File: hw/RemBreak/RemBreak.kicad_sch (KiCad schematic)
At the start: 7 parts, among them IC1 MAX17049G+T10, J1 Conn_01x03, J2 Conn_01x03, J6 Conn_01x02, SW1 SW_SPST, U1 SeeeduinoXIAO

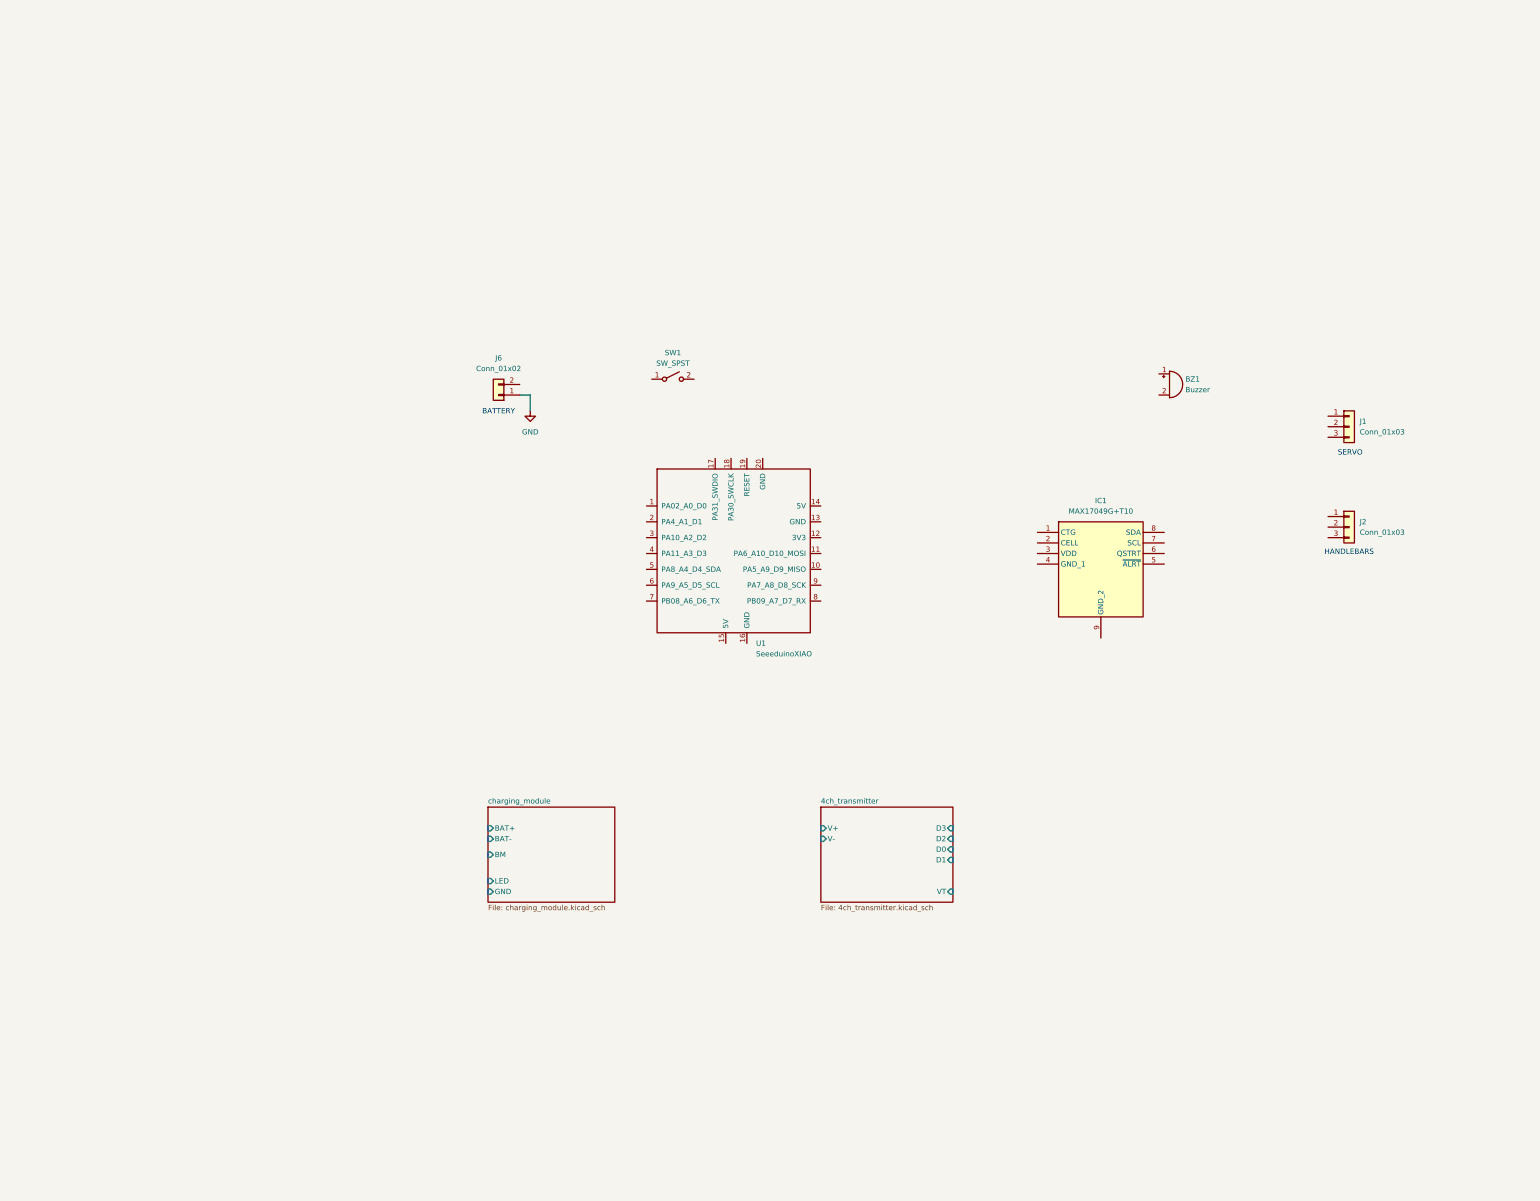
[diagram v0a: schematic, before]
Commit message: first version of the remote break main board
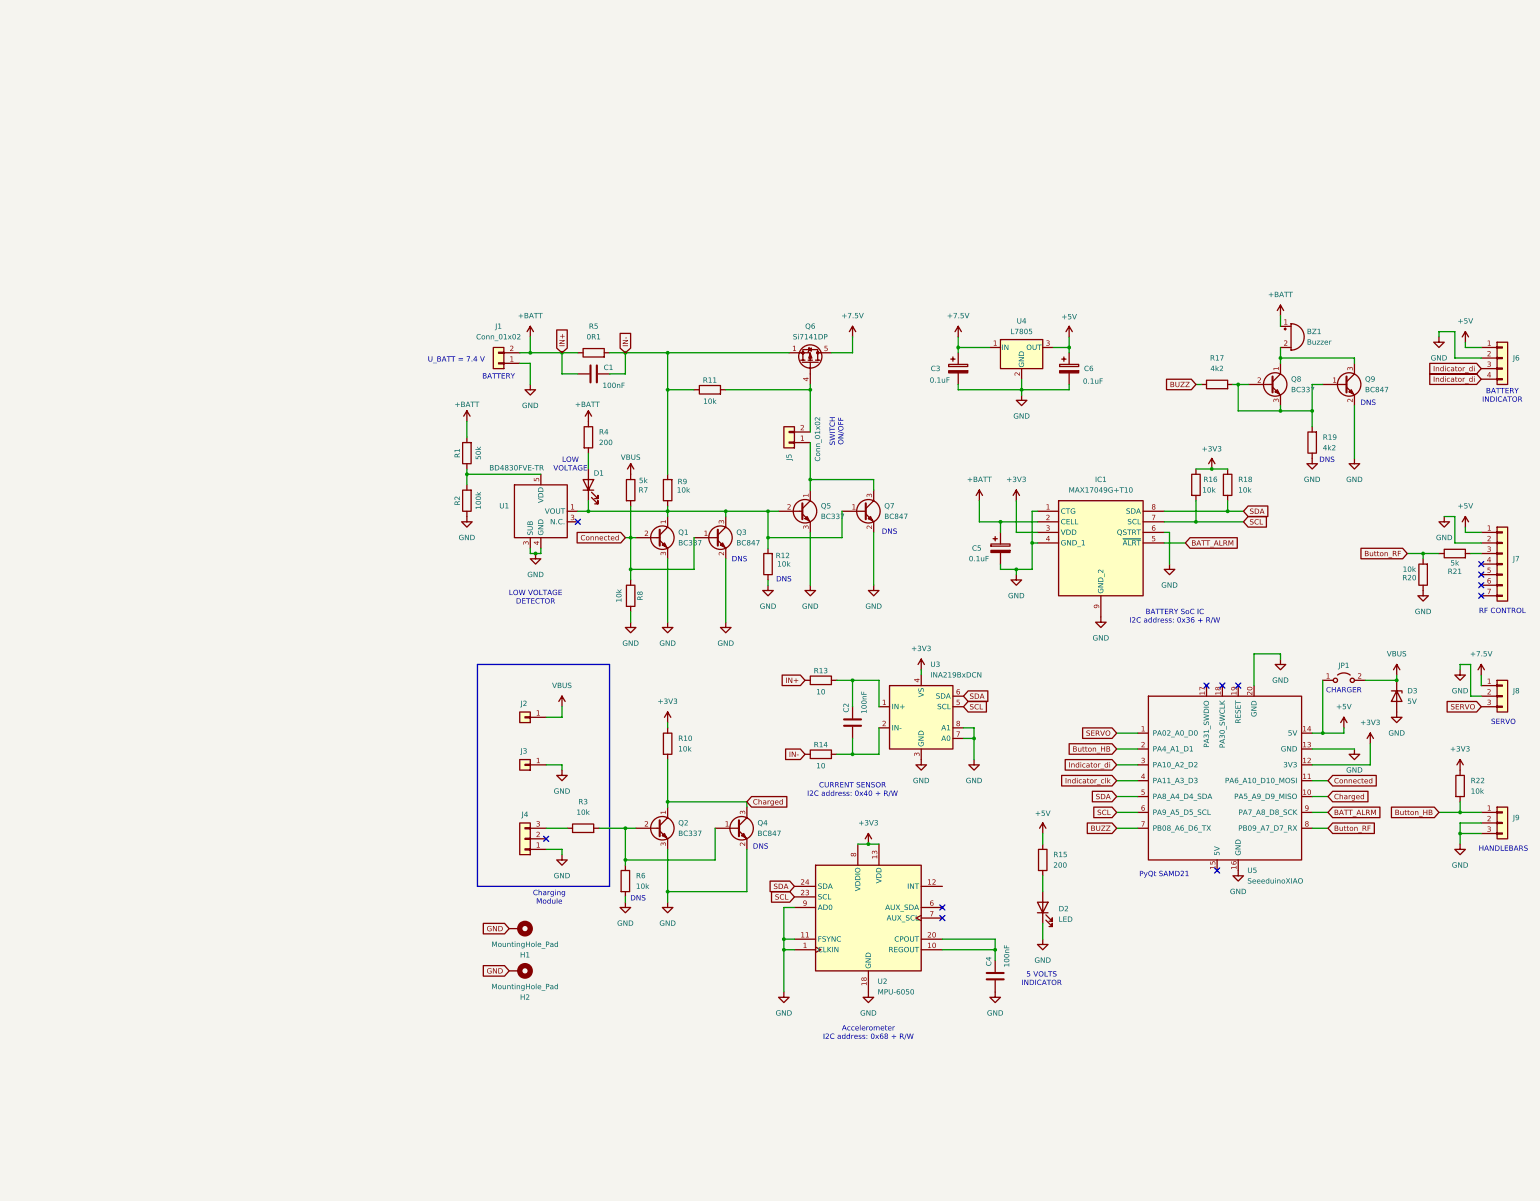
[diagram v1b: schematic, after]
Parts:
- removed SW1: SW_SPST, symbol Switch:SW_SPST
- added C1, C2, C4: 100nF, symbol Device:C
- added C3, C5, C6: 0.1uF, symbol Device:C_Polarized
- added D1, D2: LED, symbol Device:LED
- added D3: 5V, symbol Device:D_Zener
- added H1, H2: MountingHole_Pad, symbol Mechanical:MountingHole_Pad
- added J2, J3: Conn_01x01, symbol Connector_Generic:Conn_01x01
- added J4: Conn_01x03, symbol Connector_Generic:Conn_01x03
- added J5: Conn_01x02, symbol Connector_Generic:Conn_01x02
- added J6: Conn_01x04, symbol Connector_Generic:Conn_01x04
- added J7: Conn_01x07, symbol Connector_Generic:Conn_01x07
- added JP1: Jumper_2_Open, symbol Jumper:Jumper_2_Open
- added Q1, Q2, Q5, Q8: BC337, Package_TO_SOT_THT:TO-92_Inline, symbol Transistor_BJT:BC337
- added Q3, Q4, Q7, Q9: BC847, Package_TO_SOT_SMD:SOT-23, symbol Transistor_BJT:BC847
- added Q6: Si7141DP, Package_SO:PowerPAK_SO-8_Single, symbol Transistor_FET:Si7141DP
- added R1: 50k, symbol Device:R
- added R10, R11, R12, R16, R18, R20, R22, R3, R6, R8, R9: 10k, symbol Device:R
- added R13, R14: 10, symbol Device:R
- added R15, R4: 200, symbol Device:R
- added R17, R19: 4k2, symbol Device:R
- added R2: 100k, symbol Device:R
- added R21, R7: 5k, symbol Device:R
- added R5: 0R1, symbol Device:R
- added U1: BD4830FVE-TR, Package_TO_SOT_SMD:VSOF5, symbol dodo-power:BD4830FVE-TR
- added U2: MPU-6050, Sensor_Motion:InvenSense_QFN-24_4x4mm_P0.5mm, symbol Sensor_Motion:MPU-6050
- added U3: INA219BxDCN, Package_TO_SOT_SMD:SOT-23-8, symbol Analog_ADC:INA219BxDCN
- added U4: L7805, symbol Regulator_Linear:L7805
- renumbered J6 to J1, J1 to J8, J2 to J9, U1 to U5
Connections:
- net GND: now also IC1.1 (CTG), IC1.4 (GND_1), IC1.6 (QSTRT), IC1.9 (GND_2), J8.2 (Pin_2), J9.2 (Pin_2), J9.3 (Pin_3), U5.13 (GND), U5.16 (GND), U5.20 (GND), C3.2, C4.1, C5.2, C6.2, D2.1 (K), D3.2 (A), H1.1, H2.1, J3.1 (Pin_1), J4.1 (Pin_1), J6.2 (Pin_2), J7.2 (Pin_2), Q1.3 (E), Q2.3 (E), Q3.2 (E), Q4.2 (E), Q5.3 (E), Q7.2 (E), Q9.2 (E), R12.1, R19.1, R2.1, R20.1, R6.2, R8.2, U1.3 (SUB), U1.4 (GND), U2.1 (CLKIN), U2.11 (FSYNC), U2.18 (GND), U2.9 (AD0), U3.3 (GND), U3.7 (A0), U3.8 (A1), U4.2 (GND)
- net +BATT: now reaches BZ1.1 (-)
- net +BATT: now also IC1.2 (CELL), J1.2 (Pin_2), C1.1, C5.1, R1.2, R13.1, R4.1, R5.1
- net at BZ1.2 (+): now also Q8.1 (C), Q9.3 (C)
- net SERVO: now reaches U5.1 (PA02_A0_D0)
- net SERVO: now also J8.3 (Pin_3)
- net Charged: now reaches U5.10 (PA5_A9_D9_MISO)
- net Charged: now also Q2.1 (C), Q4.3 (C), R10.2
- net Connected: now reaches U5.11 (PA6_A10_D10_MOSI)
- net Connected: now also Q1.2 (B), Q3.1 (B), R7.2, R8.1
- net +3V3: now reaches U5.12 (3V3)
- net +3V3: now also IC1.3 (VDD), R10.1, R16.1, R18.1, R22.1, U2.13 (VDD), U2.8 (VDDIO), U3.4 (VS)
- net +5V: now reaches U5.14 (5V)
- net +5V: now also C6.1, J6.1 (Pin_1), J7.1 (Pin_1), JP1.1 (A), R15.1, U4.3 (OUT)
- net Button_HB: now reaches U5.2 (PA4_A1_D1)
- net Button_HB: now also J9.1 (Pin_1), R22.2
- net Indicator_di: now reaches U5.3 (PA10_A2_D2)
- net Indicator_di: now also J6.3 (Pin_3), J6.4 (Pin_4)
- net Indicator_clk: now reaches U5.4 (PA11_A3_D3)
- net SDA: now reaches U5.5 (PA8_A4_D4_SDA)
- net SDA: now also IC1.8 (SDA), R18.2, U2.24 (SDA), U3.6 (SDA)
- net SCL: now reaches U5.6 (PA9_A5_D5_SCL)
- net SCL: now also IC1.7 (SCL), R16.2, U2.23 (SCL), U3.5 (SCL)
- net BUZZ: now reaches U5.7 (PB08_A6_D6_TX)
- net BUZZ: now also R17.1
- net Button_RF: now reaches U5.8 (PB09_A7_D7_RX)
- net Button_RF: now also R20.2, R21.1
- net BATT_ALRM: now reaches U5.9 (PA7_A8_D8_SCK)
- net BATT_ALRM: now also IC1.5 (~{ALRT})
- net +7.5V: now reaches J8.1 (Pin_1)
- net +7.5V: now also C3.1, Q6.5 (D), U4.1 (IN)
- new net: J4.3 (Pin_3), R3.1
- new net: Q2.2 (B), Q4.1 (B), R3.2, R6.1
- new net: D1.1 (K), Q1.1 (C), Q3.3 (C), Q5.2 (B), Q7.1 (B), R12.2, R9.1, U1.1 (VOUT)
- new net: J5.2 (Pin_2), Q6.4 (G), R11.2
- new net: C2.1, R14.2, U3.2 (IN-)
- new net: C2.2, R13.2, U3.1 (IN+)
- new net: D1.2 (A), R4.2
- new net: R1.1, R2.2, U1.5 (VDD)
- new net: J5.1 (Pin_1), Q5.1 (C), Q7.3 (C)
- new net: D2.2 (A), R15.2
- new net: J7.3 (Pin_3), R21.2
- new net: C4.2, U2.10 (REGOUT), U2.20 (CPOUT)
- new net: Q8.2 (B), Q8.3 (E), Q9.1 (B), R17.2, R19.2
- new net IN-: C1.2, Q6.1 (S), Q6.2 (S), Q6.3 (S), R11.1, R14.1, R5.2, R9.2
- new net VBUS: D3.1 (K), J2.1 (Pin_1), JP1.2 (B), R7.1
- no-connect marks 0 -> 12
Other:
- removed sheet 4ch_transmitter
- removed sheet charging_module
- note added: "5 VOLTS INDICATOR"
- note added: "Accelerometer I2C address: 0x68 + R/W"
- note added: "BATTERY INDICATOR"
- note added: "BATTERY SoC IC I2C address: 0x36 + R/W"
- note added: "CHARGER"
- note added: "CURRENT SENSOR I2C address: 0x40 + R/W"
- note added: "Charging Module"
- note added: "DNS"
- note added: "LOW VOLTAGE"
- note added: "LOW VOLTAGE DETECTOR"
- note added: "PyQt SAMD21"
- note added: "RF CONTROL"
- note added: "SWITCH ON/OFF"
- note added: "U_BATT = 7.4 V"
- title: (none) -> Remote Break Main Board
- moved on the sheet: BZ1, IC1, J1, J8, J9, U5

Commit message: schematics supporting different pinout of BJTs and removed accelerometer
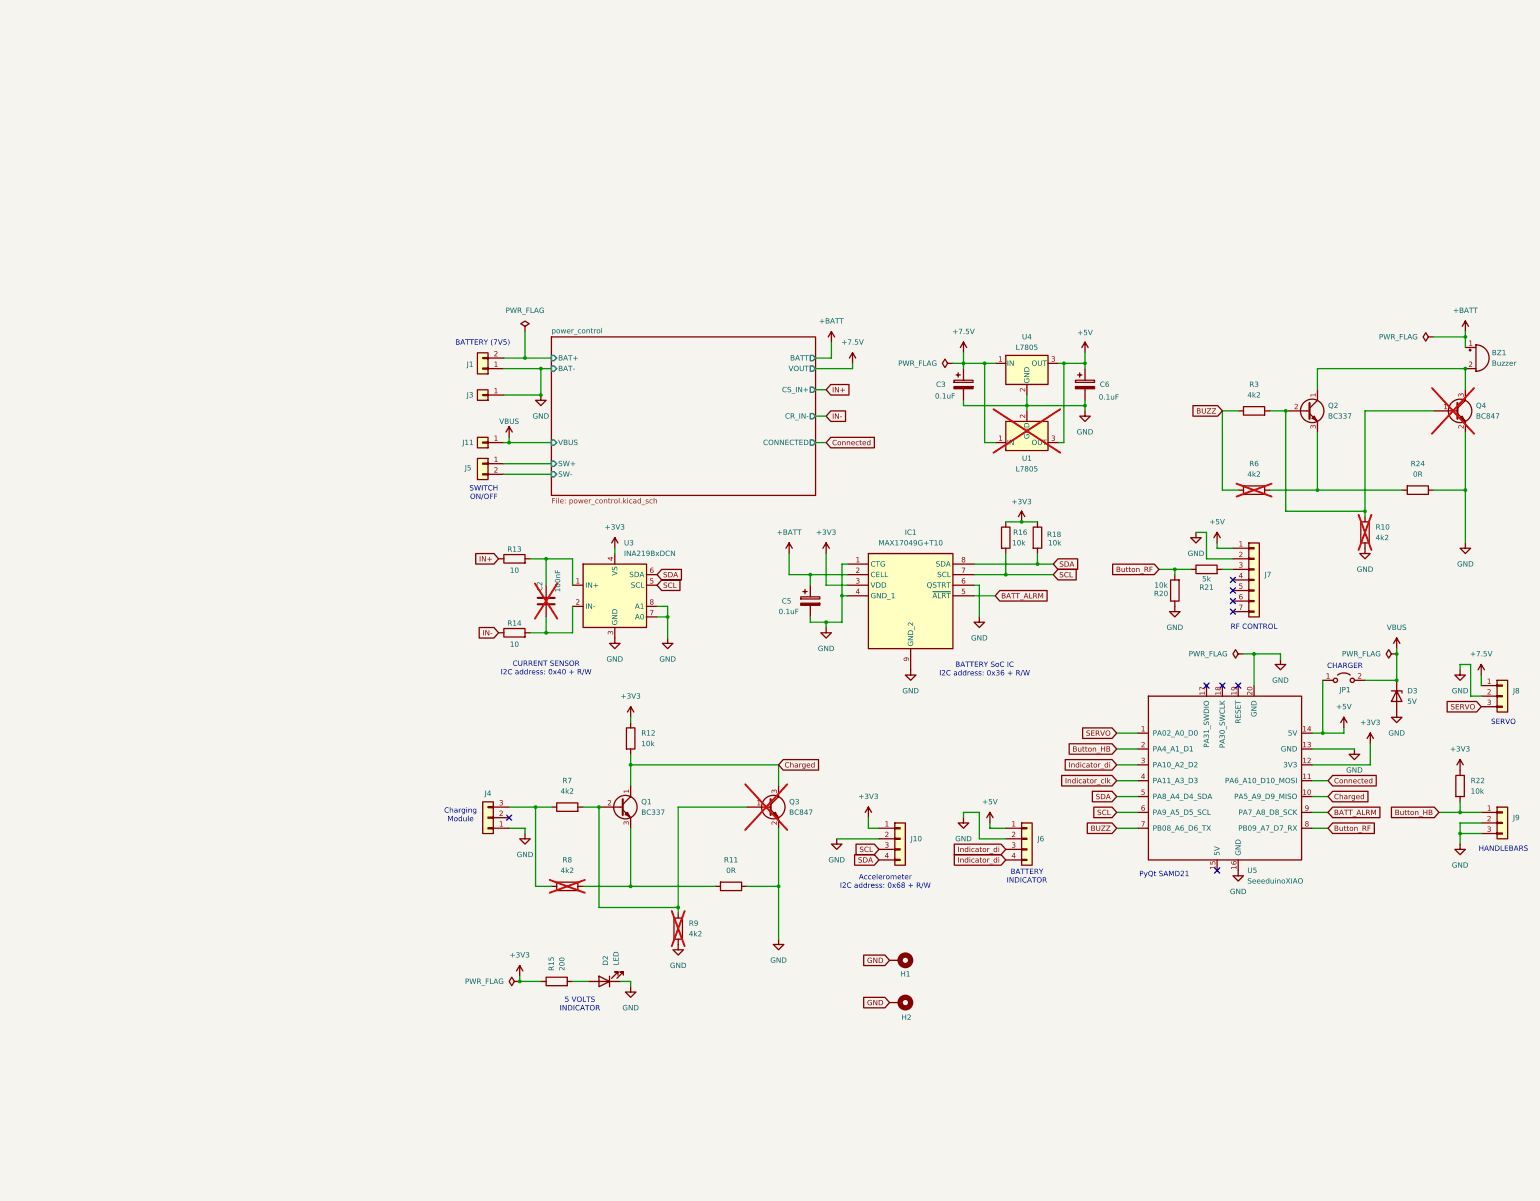
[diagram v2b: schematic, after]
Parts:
- removed C1, C4: 100nF, symbol Device:C
- removed D1: LED, symbol Device:LED
- removed J2: Conn_01x01, symbol Connector_Generic:Conn_01x01
- removed Q5, Q8: BC337, Package_TO_SOT_THT:TO-92_Inline, symbol Transistor_BJT:BC337
- removed Q6: Si7141DP, Package_SO:PowerPAK_SO-8_Single, symbol Transistor_FET:Si7141DP
- removed Q7, Q9: BC847, Package_TO_SOT_SMD:SOT-23, symbol Transistor_BJT:BC847
- removed R1: 50k, symbol Device:R
- removed R17, R19: 4k2, symbol Device:R
- removed R2: 100k, symbol Device:R
- removed R4: 200, symbol Device:R
- removed R5: 0R1, symbol Device:R
- removed U1: BD4830FVE-TR, Package_TO_SOT_SMD:VSOF5, symbol dodo-power:BD4830FVE-TR
- removed U2: MPU-6050, Sensor_Motion:InvenSense_QFN-24_4x4mm_P0.5mm, symbol Sensor_Motion:MPU-6050
- added J10: Conn_01x04, symbol Connector_Generic:Conn_01x04
- added J11: Conn_01x01, symbol Connector_Generic:Conn_01x01
- added R24: 0R, symbol Device:R
- added U1: L7805, symbol Regulator_Linear:L7805
- C2, Q3, Q4: now not fitted
- R10, R6, R8, R9: value 10k -> 4k2; now not fitted
- R11: value 10k -> 0R
- R3: value 10k -> 4k2
- R7: value 5k -> 4k2
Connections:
- net +3V3: now also R12.1, R15.1, J10.1 (Pin_1); no longer R10.1
- net +5V: now also U1.3 (OUT); no longer R15.1
- net +7.5V: now also U1.1 (IN)
- net +BATT: no longer J1.2 (Pin_2), R13.1
- net BUZZ: now also R3.1, R6.1
- net Charged: now also Q1.1 (C), Q3.3 (C), R12.2; no longer Q2.1 (C), Q4.3 (C), R10.2
- net Connected: no longer Q1.2 (B), Q3.1 (B), R7.2, R8.1
- net GND: now also R10.1, R11.1, R9.1, J10.2 (Pin_2), R24.1, U1.2 (GND); no longer Q1.3 (E), Q2.3 (E), R12.1, R6.2, R8.2
- net IN-: no longer R11.1, R9.2
- net SCL: now also J10.3 (Pin_3)
- net SDA: now also J10.4 (Pin_4)
- net VBUS: now also J11.1 (Pin_1); no longer R7.1
- net at J4.3 (Pin_3): now also R7.1, R8.1; no longer R3.1
- net at Q2.2 (B), Q4.1 (B), R3.2: now also R10.2; no longer R6.1
- net at R11.2: now also Q1.3 (E), R8.2; no longer J5.2 (Pin_2)
- net at BZ1.2 (+): now also Q2.1 (C), Q4.3 (C)
- net power_control/SW+: now reaches J5.1 (Pin_1)
- new net: Q2.3 (E), R24.2, R6.2
- new net: Q1.2 (B), Q3.1 (B), R7.2, R9.2
- new net IN+: R13.1
- new net power_control/BAT+: J1.2 (Pin_2)
- new net power_control/SW-: J5.2 (Pin_2)
- no-connect marks 12 -> 9
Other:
- added sheet power_control (power_control.kicad_sch)
- note added: "BATTERY (7V5)"
- note removed: "BATTERY"
- note removed: "DNS"
- note removed: "LOW VOLTAGE"
- note removed: "LOW VOLTAGE DETECTOR"
- note removed: "U_BATT = 7.4 V"
- moved on the sheet: BZ1, C3, C5, C6, D2, H1, H2, IC1, J1, J3, J4, J5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
